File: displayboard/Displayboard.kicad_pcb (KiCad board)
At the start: 2 copper layers, 106 x 80 mm, 27 parts, among them IC401 PCAL6416AHF, Q501 NPN, SW401 Button 1, SW402 Button 2, SW403 Button 3, SW404 Button 4, X501 Touch, X502 Display, X503 Mainboard

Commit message: Feature: Issue #19
- Replace JS1400BFQ with MU-BUE70R
- Add CI/CD workflow to check for changelog updates on PRs

Closes #19

Signed-off-by: Daniel Kampert <DanielKampert@kampis-elektroecke.de>
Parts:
- S401: value JS1400 -> NAVIGATION
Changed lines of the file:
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@@
 			)
 		)
-		(property "Value" "JS1400"
+		(property "Value" "NAVIGATION"
 			(at 0 0 135)
 			(layer "F.SilkS")
@@
 			)
 		)
-		(property "Datasheet" "https://configured-product-images.s3.amazonaws.com/2D/specs/JS1400BVQ.pdf"
+		(property "Datasheet" "https://www.apem.com/de/medias/download/PCB_MU_serie.pdf"
 			(at 0 0 135)
 			(layer "F.Fab")
@@
 			)
 		)
-		(property "manf" "E-Switch"
+		(property "manf" "Apem"
 			(at 0 0 315)
 			(unlocked yes)
@@
 			)
 		)
-		(property "manf#" "JS1400"
+		(property "manf#" "MU-BUE70R"
 			(at 0 0 315)
 			(unlocked yes)
@@
 			)
 		)
-		(property "mouser#" "612-JS1400"
+		(property "mouser#" "642-MU-BUE70R"
 			(at 0 0 315)
 			(unlocked yes)

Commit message: Added: Add a cutout for the display cable, add different assembly improvements
Signed-off-by: Daniel Kampert <DanielKampert@kampis-elektroecke.de>
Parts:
- added R505: 0R, Resistor_SMD:R_0805_2012Metric, B.Cu at (208.5, 124.2)
- D401: value STATUS -> Status
- Q501: value NPN -> BC817W
- S401: value NAVIGATION -> Navigation
- moved R504 0.10 mm to (212.1, 124.2)
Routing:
- net Net-(Q501-B): track 4.27 -> 6.49 mm
- net +3V3: track 9.78 -> 10.6 mm, vias 8 -> 9
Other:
- outline, holes or cut-outs redrawn

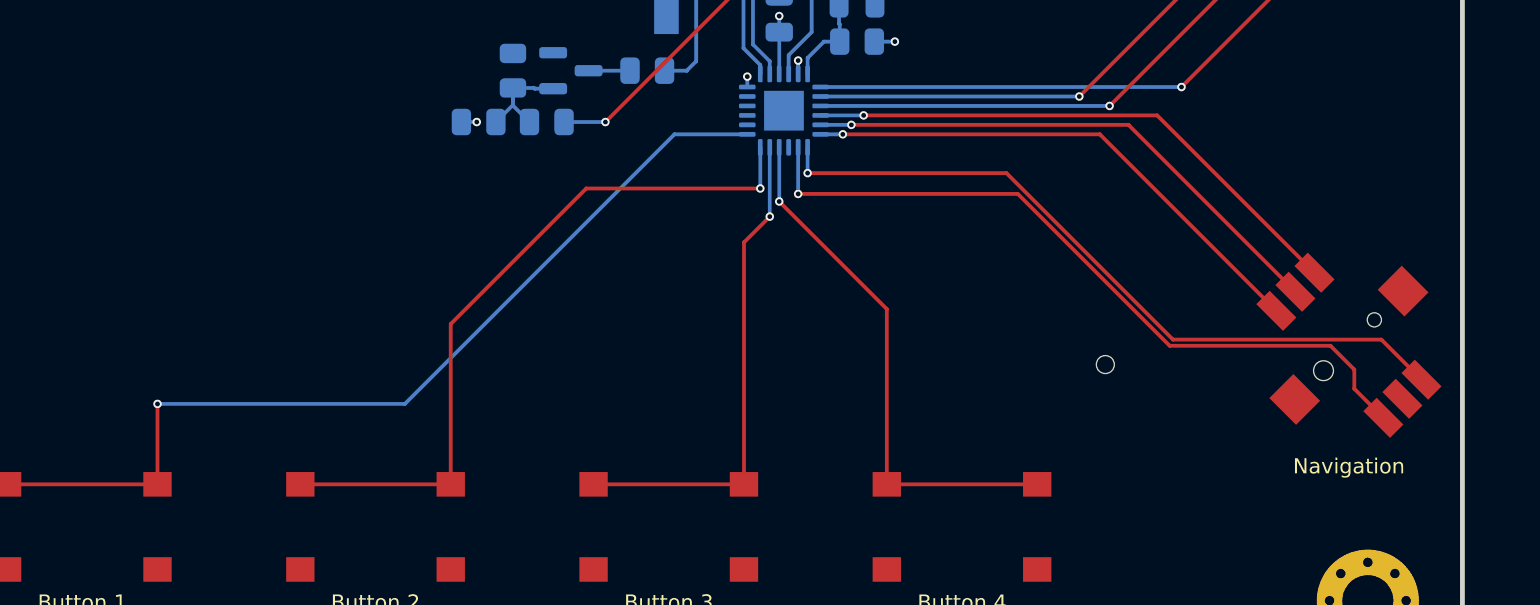
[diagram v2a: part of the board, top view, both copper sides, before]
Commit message: Feature: Add debounce capacitors to push buttons
- Replace NPN transistor with N-Channel MOSFET

Signed-off-by: Daniel Kampert <DanielKampert@kampis-elektroecke.de>
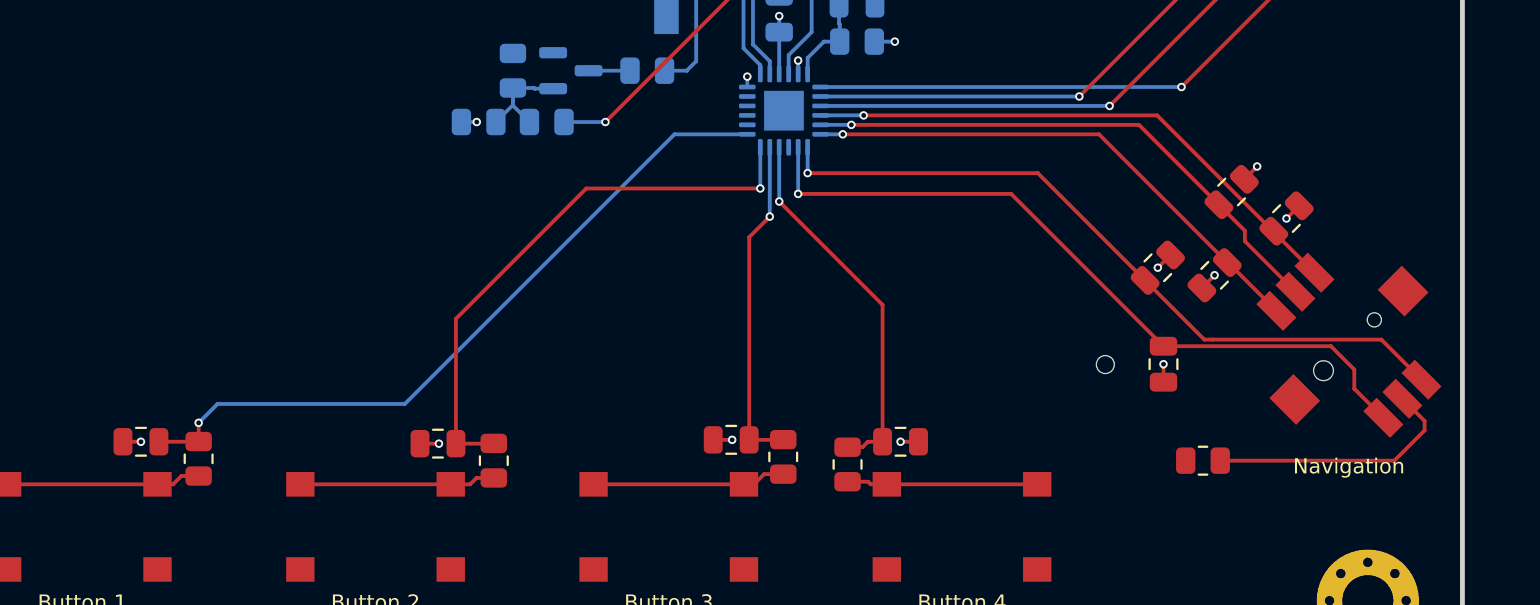
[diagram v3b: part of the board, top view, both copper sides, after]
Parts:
- added C403: 100n, Capacitor_SMD:C_0805_2012Metric, F.Cu at (230.8, 141.1)
- added C404: 100n, Capacitor_SMD:C_0805_2012Metric, F.Cu at (221.8, 141.0)
- added C405: 100n, Capacitor_SMD:C_0805_2012Metric, F.Cu at (206.3, 141.2)
- added C406: 100n, Capacitor_SMD:C_0805_2012Metric, F.Cu at (190.7, 141.1)
- added C407: 100n, Capacitor_SMD:C_0805_2012Metric, F.Cu at (247.4, 132.3)
- added C408: 100n, Capacitor_SMD:C_0805_2012Metric, F.Cu at (244.7, 137.0)
- added C409: 100n, Capacitor_SMD:C_0805_2012Metric, F.Cu at (244.4, 131.9)
- added C410: 100n, Capacitor_SMD:C_0805_2012Metric, F.Cu at (248.3, 127.9)
- added C411: 100n, Capacitor_SMD:C_0805_2012Metric, F.Cu at (251.2, 129.3)
- added R406: 1k, Resistor_SMD:R_0805_2012Metric, F.Cu at (193.7, 142.0)
- added R407: 1k, Resistor_SMD:R_0805_2012Metric, F.Cu at (209.3, 142.1)
- added R408: 1k, Resistor_SMD:R_0805_2012Metric, F.Cu at (224.6, 141.9)
- added R409: 1k, Resistor_SMD:R_0805_2012Metric, F.Cu at (228.0, 142.3)
- added R410: 1k, Resistor_SMD:R_0805_2012Metric, F.Cu at (246.8, 142.1)
- R504: value 100R -> 0R
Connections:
- S401 pad 5: +3V3 -> Net-(R410-Pad2)
- SW401 pad 1: Net-(IC401-P1_3) -> Net-(R406-Pad1)
- SW401 pad 3: Net-(IC401-P1_3) -> Net-(R406-Pad1)
- SW402 pad 1: Net-(IC401-P1_2) -> Net-(R407-Pad1)
- SW402 pad 3: Net-(IC401-P1_2) -> Net-(R407-Pad1)
- SW403 pad 1: Net-(IC401-P1_1) -> Net-(R408-Pad1)
- SW403 pad 3: Net-(IC401-P1_1) -> Net-(R408-Pad1)
- SW404 pad 1: Net-(IC401-P1_0) -> Net-(R409-Pad1)
- SW404 pad 3: Net-(IC401-P1_0) -> Net-(R409-Pad1)
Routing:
- net Net-(R410-Pad2): track 0.00 -> 13.6 mm
- net Net-(IC401-P1_3): track 49.3 -> 38.5 mm
- net Net-(R407-Pad1): track 0.00 -> 10.4 mm
- net Net-(R406-Pad1): track 0.00 -> 10.3 mm
- net Net-(R408-Pad1): track 0.00 -> 10.2 mm
- net Net-(R409-Pad1): track 0.00 -> 10.1 mm
- net GND: track 0.00 -> 8.66 mm, vias 0 -> 9
- net Net-(IC401-P1_1): track 26.3 -> 17.7 mm
- net Net-(IC401-P1_0): track 28.1 -> 19.8 mm
- net Net-(IC401-P1_2): track 37.9 -> 29.7 mm

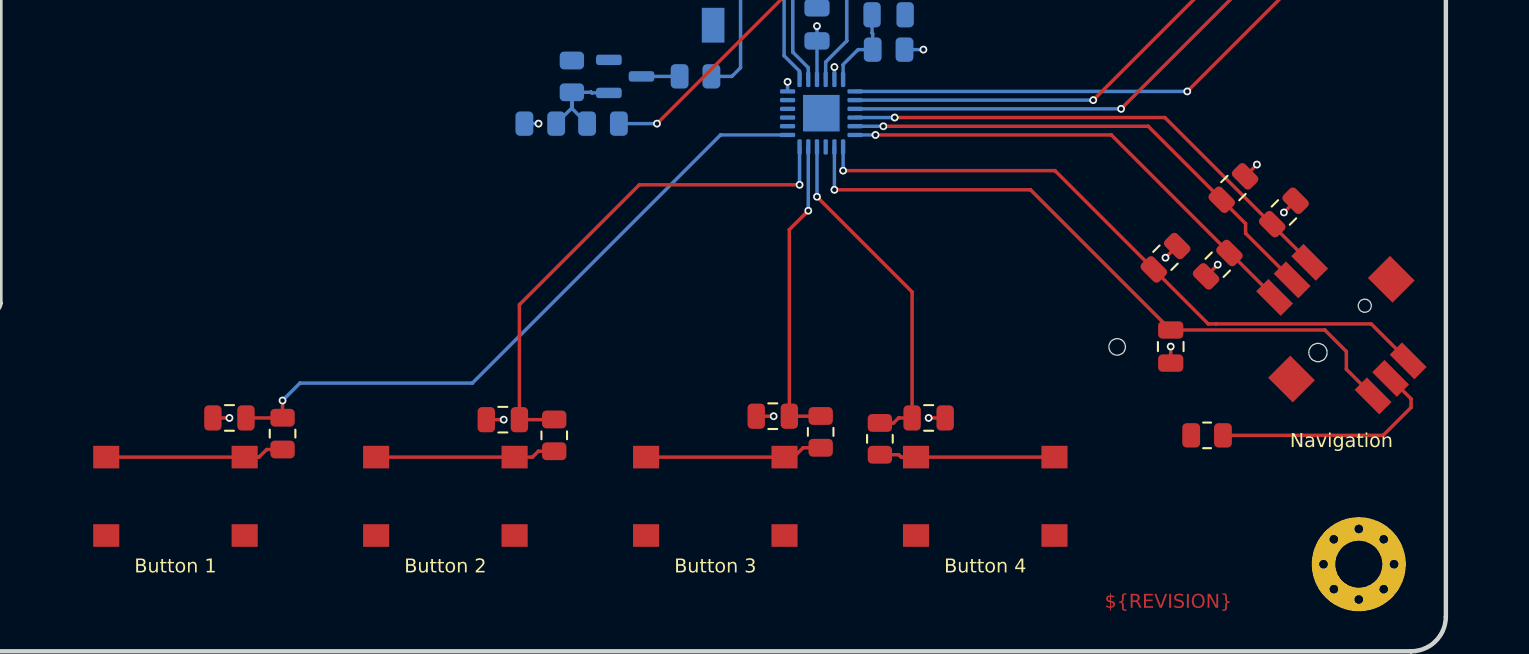
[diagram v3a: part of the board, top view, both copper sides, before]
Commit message: Changed: Rework debouncing logic
Signed-off-by: Daniel Kampert <DanielKampert@kampis-elektroecke.de>
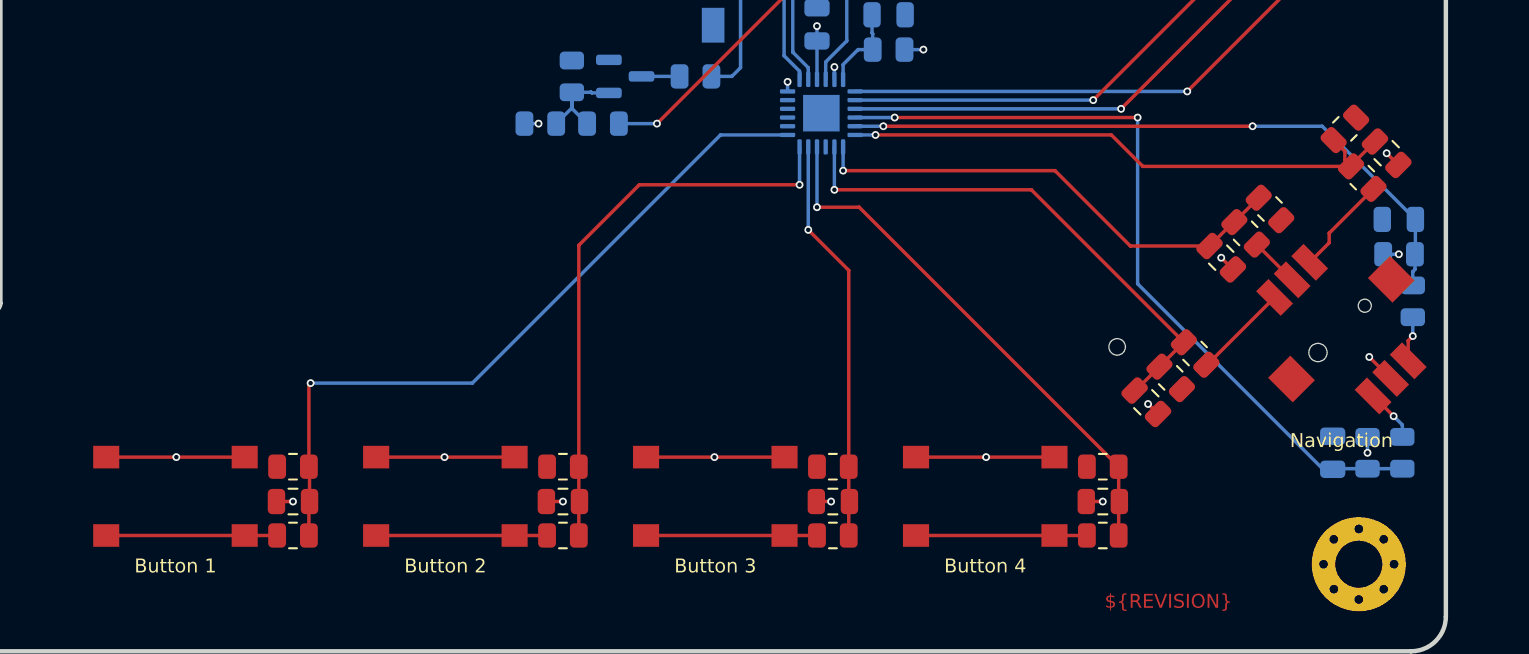
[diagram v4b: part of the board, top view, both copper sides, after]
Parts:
- removed C407, C408, C409, C410, C411: 100n, Capacitor_SMD:C_0805_2012Metric
- added C412: 100n, Capacitor_SMD:C_0805_2012Metric, F.Cu at (243.3, 140.2)
- added C413: 100n, Capacitor_SMD:C_0805_2012Metric, B.Cu at (254.0, 143.1)
- added C414: 100n, Capacitor_SMD:C_0805_2012Metric, B.Cu at (257.8, 129.7)
- added C415: 100n, Capacitor_SMD:C_0805_2012Metric, F.Cu at (257.1, 125.9)
- added C416: 100n, Capacitor_SMD:C_0805_2012Metric, F.Cu at (247.6, 131.9)
- added R411: 1k, Resistor_SMD:R_0805_2012Metric, F.Cu at (194.3, 147.8)
- added R412: 1k, Resistor_SMD:R_0805_2012Metric, F.Cu at (209.8, 147.8)
- added R413: 1k, Resistor_SMD:R_0805_2012Metric, F.Cu at (225.3, 147.8)
- added R414: 1k, Resistor_SMD:R_0805_2012Metric, F.Cu at (240.8, 147.8)
- added R415: 1k, Resistor_SMD:R_0805_2012Metric, F.Cu at (246.1, 137.4)
- added R416: 1k, Resistor_SMD:R_0805_2012Metric, B.Cu at (256.0, 143.1)
- added R417: 1k, Resistor_SMD:R_0805_2012Metric, B.Cu at (258.0, 143.1)
- added R418: 1k, Resistor_SMD:R_0805_2012Metric, B.Cu at (257.8, 131.7)
- added R419: 1k, Resistor_SMD:R_0805_2012Metric, B.Cu at (258.6, 134.4)
- added R420: 1k, Resistor_SMD:R_0805_2012Metric, F.Cu at (254.7, 124.5)
- added R421: 1k, Resistor_SMD:R_0805_2012Metric, F.Cu at (255.7, 127.3)
- added R422: 1k, Resistor_SMD:R_0805_2012Metric, F.Cu at (249.0, 130.5)
- added R423: 1k, Resistor_SMD:R_0805_2012Metric, F.Cu at (250.4, 129.1)
- R406, R407, R408, R409: value 1k -> 10k
- moved R409 12.9 mm to (240.8, 143.9), turned to 0 degrees
- moved C403 11.1 mm to (240.8, 145.9), turned to 180 degrees
- moved C406 6.03 mm to (194.3, 145.9)
- moved C404 5.99 mm to (225.3, 145.9)
- moved C405 5.83 mm to (209.8, 145.9)
- moved R410 3.90 mm to (244.7, 138.8), turned to 135 degrees
- moved R408 2.12 mm to (225.3, 143.9), turned to 0 degrees
- moved R406 1.99 mm to (194.3, 143.9), turned to 0 degrees
- moved R407 1.87 mm to (209.8, 143.9), turned to 0 degrees
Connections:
- R406 pad 1: Net-(R406-Pad1) -> +3V3
- R407 pad 1: Net-(R407-Pad1) -> +3V3
- R408 pad 1: Net-(R408-Pad1) -> +3V3
- R409 pad 1: Net-(R409-Pad1) -> +3V3
- R410 pad 2: Net-(R410-Pad2) -> Net-(IC401-P0_7)
- S401 pad 1: Net-(IC401-P0_3) -> Net-(R421-Pad1)
- S401 pad 2: Net-(IC401-P0_4) -> Net-(R422-Pad1)
- S401 pad 3: Net-(IC401-P0_5) -> Net-(R415-Pad2)
- S401 pad 4: Net-(IC401-P0_6) -> Net-(R419-Pad1)
- S401 pad 5: Net-(R410-Pad2) -> GND
- S401 pad 6: Net-(IC401-P0_7) -> Net-(R417-Pad1)
- SW401 pad 1: Net-(R406-Pad1) -> GND
- SW401 pad 2: +3V3 -> Net-(R411-Pad2)
- SW401 pad 3: Net-(R406-Pad1) -> GND
- SW401 pad 4: +3V3 -> Net-(R411-Pad2)
- SW402 pad 1: Net-(R407-Pad1) -> GND
- SW402 pad 2: +3V3 -> Net-(R412-Pad2)
- SW402 pad 3: Net-(R407-Pad1) -> GND
- SW402 pad 4: +3V3 -> Net-(R412-Pad2)
- SW403 pad 1: Net-(R408-Pad1) -> GND
- SW403 pad 2: +3V3 -> Net-(R413-Pad2)
- SW403 pad 3: Net-(R408-Pad1) -> GND
- SW403 pad 4: +3V3 -> Net-(R413-Pad2)
- SW404 pad 1: Net-(R409-Pad1) -> GND
- SW404 pad 2: +3V3 -> Net-(R414-Pad2)
- SW404 pad 3: Net-(R409-Pad1) -> GND
- SW404 pad 4: +3V3 -> Net-(R414-Pad2)
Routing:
- net GND: track 8.66 -> 40.5 mm, vias 9 -> 12
- net Net-(IC401-P0_3): track 29.6 -> 45.4 mm, vias 1 -> 2
- net Net-(R410-Pad2): track 13.6 -> 0.00 mm
- net Net-(IC401-P1_0): track 19.8 -> 30.9 mm
- net Net-(R407-Pad1): track 10.4 -> 0.00 mm
- net Net-(R406-Pad1): track 10.3 -> 0.00 mm
- net Net-(R408-Pad1): track 10.2 -> 0.00 mm
- net Net-(IC401-P0_6): track 38.3 -> 28.2 mm
- net Net-(R409-Pad1): track 10.1 -> 0.00 mm
- net Net-(R414-Pad2): track 0.00 -> 9.81 mm
- net Net-(R413-Pad2): track 0.00 -> 9.81 mm
- net Net-(R412-Pad2): track 0.00 -> 9.81 mm
- net Net-(R411-Pad2): track 0.00 -> 9.81 mm
- net Net-(IC401-P0_4): track 29.1 -> 38.2 mm, vias 1 -> 2
- net Net-(IC401-P0_7): track 38.9 -> 30.1 mm
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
